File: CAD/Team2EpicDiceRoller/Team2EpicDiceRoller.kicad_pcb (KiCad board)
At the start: 2 copper layers, 90 x 110 mm, 68 parts, among them J1 Conn_02x03_Odd_Even, J2 Conn_01x16, J3 Barrel_Jack, Q1 BSS138, SW1 SW_Toggle_SPDT, SW2 Tilt_Switch, SW3 SW_Power, SW4 RotaryEncoder_Switch, SW5 SW_LeftMenu, SW6 SW_MidMenu, SW7 SW_Reset, SW8 SW_RightMenu, U1 MC34063AD, U2 74HC14, U3 MC34063AD, U4 ATmega328P-P, Y1 Crystal_16MHz

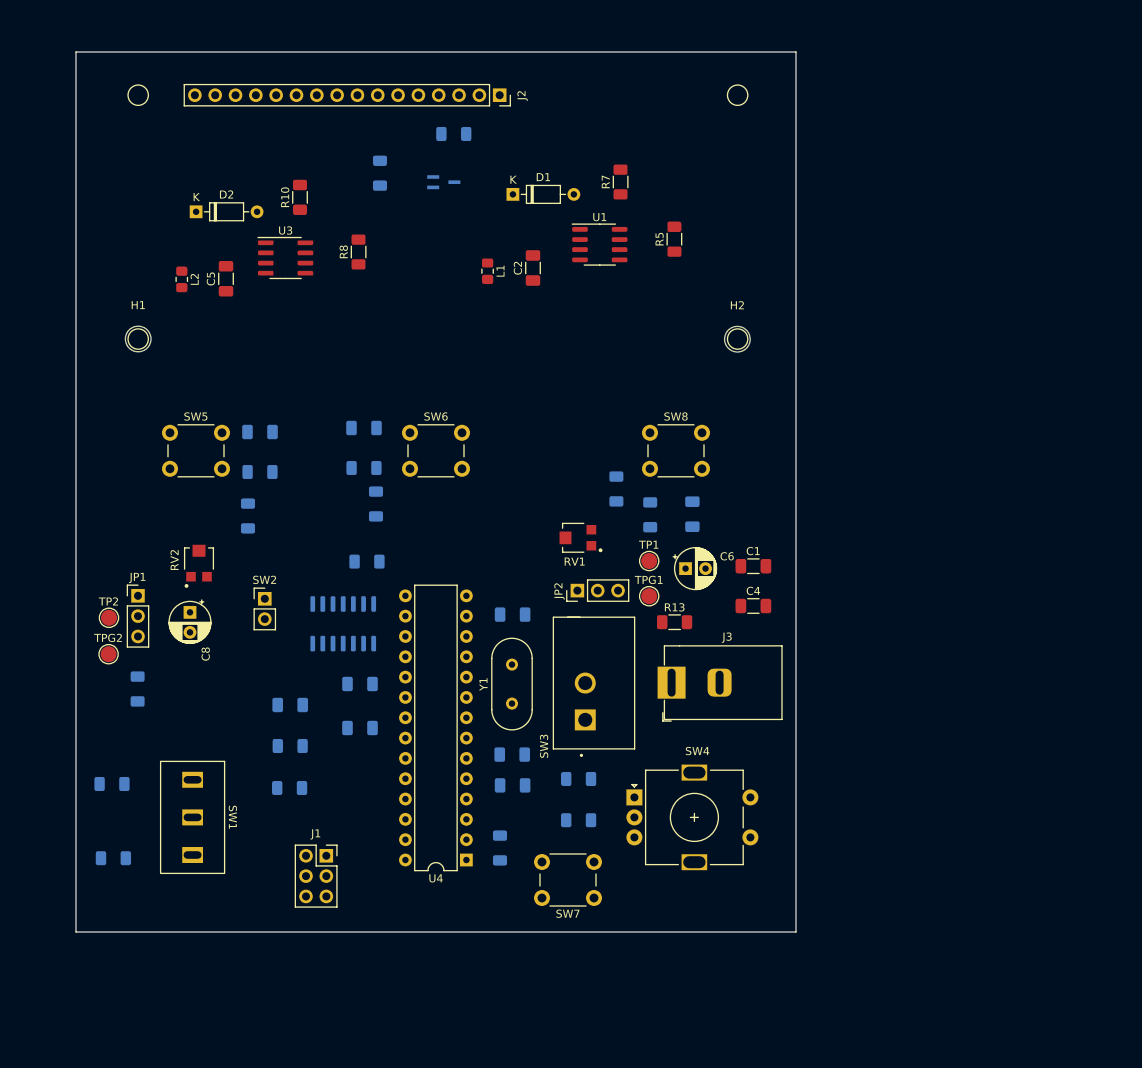
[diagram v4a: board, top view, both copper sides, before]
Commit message: Added cap, moved pots, many changes
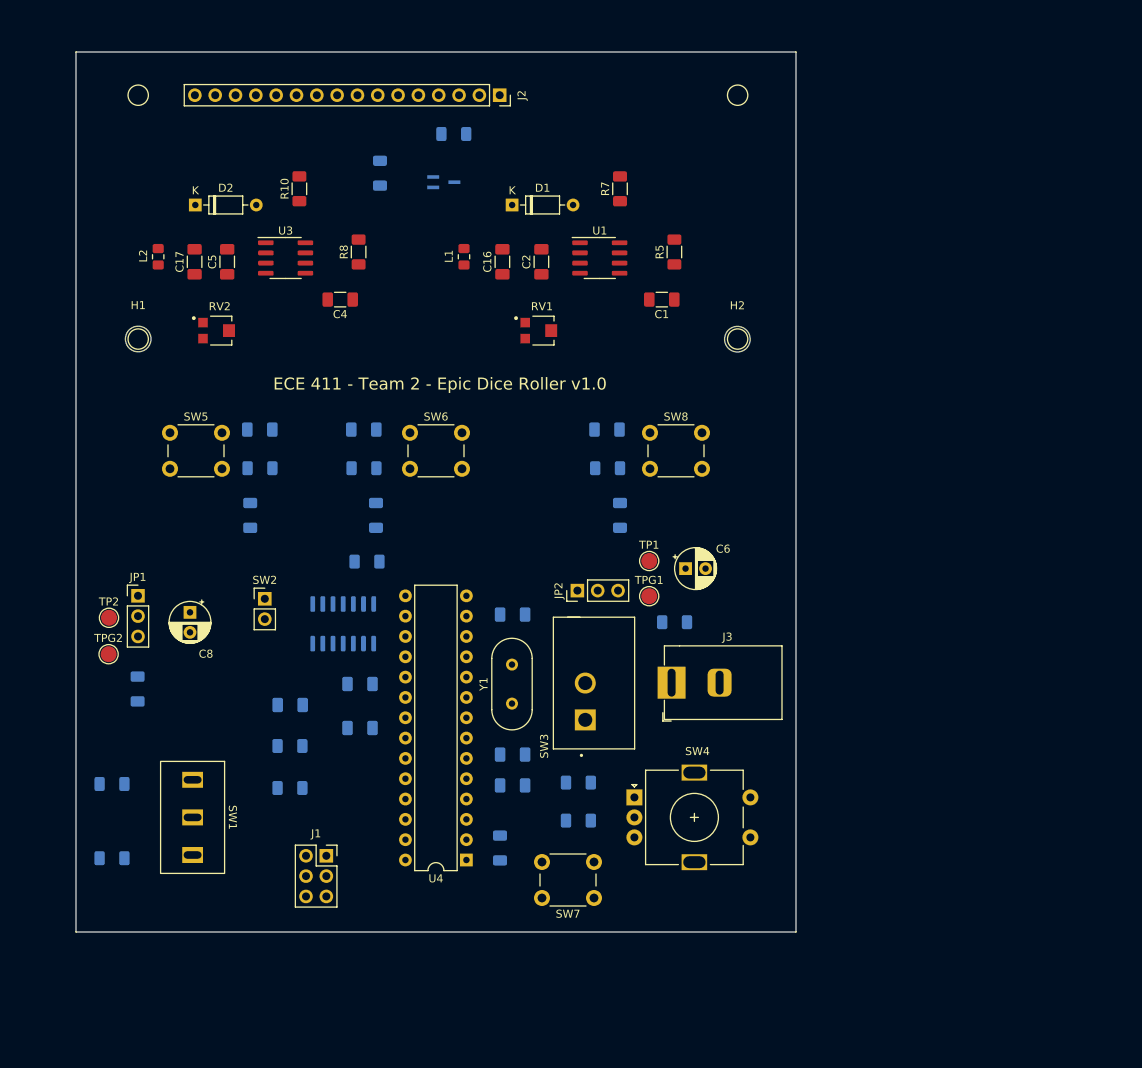
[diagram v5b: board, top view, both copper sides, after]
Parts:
- added C16: 10u, Capacitor_SMD:C_1206_3216Metric_Pad1.33x1.80mm_HandSolder, F.Cu at (150.3, 46.2)
- added C17: 10u, Capacitor_SMD:C_1206_3216Metric_Pad1.33x1.80mm_HandSolder, F.Cu at (111.8, 46.2)
- R13: moved to B.Cu
- moved C4 64.3 mm to (130.0, 51.0), turned to 180 degrees
- moved C1 35.2 mm to (170.2, 51.0), turned to 180 degrees
- moved RV2 29.1 mm to (114.7, 54.8), turned to 0 degrees
- moved RV1 26.3 mm to (154.9, 54.8), turned to 0 degrees
- moved C12 15.0 mm to (163.4, 67.2), turned to 0 degrees
- moved R20 7.89 mm to (163.4, 72.0), turned to 180 degrees
- moved R21 5.20 mm to (159.8, 116.1)
- moved R22 4.70 mm to (159.8, 111.3)
- moved L2 4.09 mm to (107.3, 45.6)
- moved L1 3.46 mm to (145.5, 45.6)
- moved R19 3.33 mm to (165.0, 77.9)
- moved C5 2.13 mm to (115.9, 46.2)
- moved U1 1.67 mm to (162.5, 45.8)
- moved R5 1.60 mm to (171.8, 45.0)
- moved R15 1.42 mm to (134.5, 77.9)
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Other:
- board text added: "ECE 411 - Team 2 - Epic Dice Roller v1.0"

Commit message: Updated silk screen, ready to route
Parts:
- added H3: MountingHole, MountingHole:MountingHole_3.2mm_M3, F.Cu at (104.8, 25.4)
- added H4: MountingHole, MountingHole:MountingHole_3.2mm_M3, F.Cu at (179.7, 25.4)
- moved SW2 30.3 mm to (150.7, 85.2), turned to 90 degrees
- moved R1 19.1 mm to (152.2, 80.9), turned to 180 degrees
- moved R21 5.03 mm to (159.8, 111.0)
- moved R22 4.58 mm to (159.8, 115.9)
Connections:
- R21 pad 2: IO2_PD2 -> IO3_PD3
- R22 pad 1: IO3_PD3 -> IO2_PD2
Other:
- board text added: "3V3 ADJ"
- board text added: "5V ADJ"
- board text added: "LOAD 3V3 LV"
- board text added: "M3"
- board text added: "MISO SCK RESET#"
- board text added: "MOSI GND"
- board text added: "RESET"
- board text added: "RX"
- board text added: "VCC 5V LOAD"
- board text added: "VCC GND"

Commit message: Updated silk screen, ready to route
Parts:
- moved R3 0.58 mm to (101.6, 110.9)
- moved R2 0.38 mm to (101.6, 120.4)
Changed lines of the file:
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@@
   )
   (footprint "Resistor_SMD:R_1206_3216Metric_Pad1.30x1.75mm_HandSolder" (layer "B.Cu")
-    (at 101.5 120.775)
+    (at 101.575 120.4)
     (descr "Resistor SMD 1206 (3216 Metric), square (rectangular) end terminal, IPC_7351 nominal with elongated pad for handsoldering. (Body size source: IPC-SM-782 page 72, https://www.pcb-3d.com/wordpress/wp-content/uploads/ipc-sm-782a_amendment_1_and_2.pdf), generated with kicad-footprint-generator")
     (tags "resistor handsolder")
@@
   )
   (footprint "Resistor_SMD:R_1206_3216Metric_Pad1.30x1.75mm_HandSolder" (layer "B.Cu")
-    (at 101.5 111.5)
-    (descr "Resistor SMD 1206 (3216 Metric), square (rectangular) end terminal, IPC_7351 nominal with elongated pad for handsoldering. (Body size source: IPC-SM-782 page 72, https://www.pcb-3d.com/wordpress/wp-content/uploads/ipc-sm-782a_amendment_1_and_2.pdf), generated with kicad-footprint-generator")
-    (tags "resistor handsolder")
+    (at 101.575 110.925)
+    (descr "Resistor SMD 1206 (3216 Metric), square (rectangular) end terminal, IPC_7351 nominal with elongated pad for handsoldering. (Body size source: IPC-SM-782 page 72, https://www.pcb-3d.com/wordpress/wp-content/uploads/ipc-sm-782a_amendment_1_and_2.pdf), generated with kicad-footprint-generator")
+    (tags "resistor handsolder")

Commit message: drew's layout. Still working on ground and final touches
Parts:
- moved R15 2.76 mm to (132.0, 79.0)
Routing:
- net VCC: track 0.00 -> 201.2 mm, vias 0 -> 3
- net /Vin: track 0.00 -> 138.3 mm
- net Net-(R4-Pad2): track 0.00 -> 94.3 mm
- net +3V3: track 0.00 -> 81.5 mm
- net IO8_PB0: track 0.00 -> 63.9 mm, vias 0 -> 2
- net /3V3: track 0.00 -> 62.5 mm
- net AD0_PC0: track 0.00 -> 60.5 mm
- net /RigDebn: track 0.00 -> 42.7 mm
- net AD1_PC1: track 0.00 -> 39.0 mm
- net IO11_MOSI_PB3: track 0.00 -> 35.1 mm
- net IO13_SCK_PB5: track 0.00 -> 29.0 mm
- net IO12_MISO_PB4: track 0.00 -> 29.0 mm
- net RESET#: track 0.00 -> 29.0 mm
- net /LeftDebn: track 0.00 -> 23.9 mm
- net IO5_PD5: track 0.00 -> 21.1 mm
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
